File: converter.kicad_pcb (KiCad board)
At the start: 2 copper layers, 26 x 37 mm, 61 parts, among them CN1 MINI_DIN_8P_JACK, J1 USB_mini_micro_B, P1 CONN_1, P2 CONN_1, P3 CONN_1, P4 CONN_1, SW1 SW_PUSH, U1 ATMEGA32U2, X1 16MHz

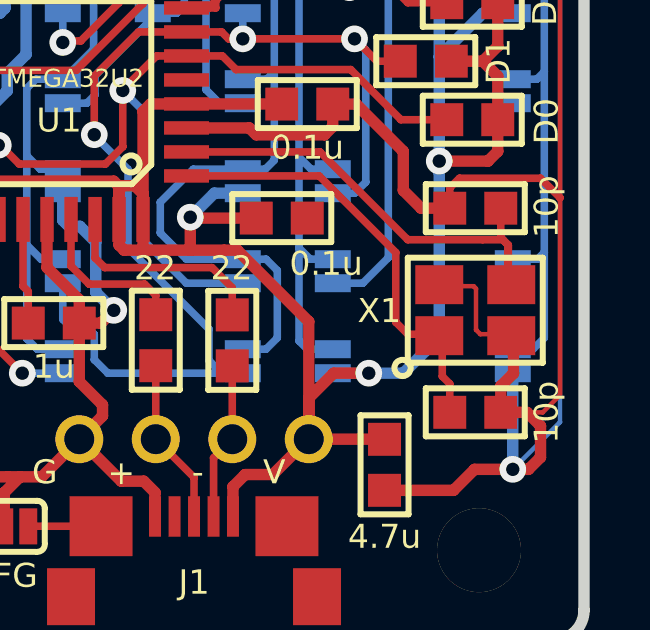
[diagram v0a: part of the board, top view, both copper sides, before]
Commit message: Change foot print of Xtal
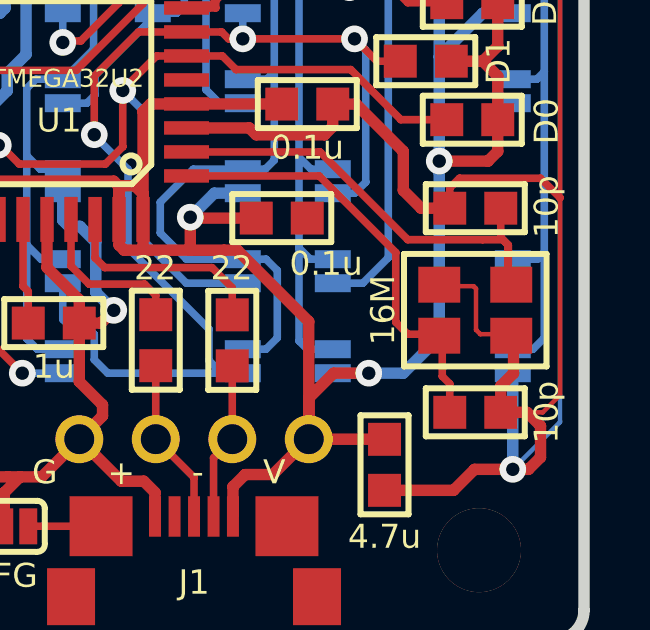
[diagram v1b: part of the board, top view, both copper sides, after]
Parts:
- X1: value 16MHz -> 16M; footprint 000NewKeyboard_parts:FA-238 -> keyboard_parts:FA-238
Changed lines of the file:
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@@
-(kicad_pcb (version 4) (host pcbnew no-vcs-found-product)
+(kicad_pcb (version 4) (host pcbnew 4.0.2+e4-6225~38~ubuntu16.04.1-stable)
   (general
     (links 112)
     (no_connects 0)
-    (area 94.297601 94.83508 130.537334 138.654001)
+    (area 94.297601 89.83508 137.637115 142.419201)
     (thickness 1.6002)
     (drawings 60)
@@
     (add_net GND)
   )
+  (module keyboard_parts:FA-238 (layer Front)
+    (at 122.375 126)
+    (fp_text reference X1 (at 0 2.55) (layer F.SilkS) hide
+      (effects (font (size 0.8 0.8) (thickness 0.15)))
+    )
+    (fp_text value 16M (at -3.075 0 90) (layer F.SilkS)
+      (effects (font (size 0.8 0.8) (thickness 0.15)))
+    )
+    (fp_line (start -2.375 1.875) (end -2.375 -1.875) (layer F.SilkS) (width 0.2))
+    (fp_line (start -2.375 -1.875) (end 2.375 -1.875) (layer F.SilkS) (width 0.2))
+    (fp_line (start 2.375 -1.875) (end 2.375 1.875) (layer F.SilkS) (width 0.2))
+    (fp_line (start 2.375 1.875) (end -2.375 1.875) (layer F.SilkS) (width 0.2))
+    (pad 3 smd rect (at -1.1 -0.8) (size 1.4 1.2) (drill (offset -0.1 -0.05)) (layers Front F.Paste F.Mask)
+      (net 31 GND) (clearance 0.2))
+    (pad 2 smd rect (at 1.1 -0.8) (size 1.4 1.2) (drill (offset 0.1 -0.05)) (layers Front F.Paste F.Mask)
+      (net 34 "Net-(C6-Pad1)") (clearance 0.2))
+    (pad 1 smd rect (at -1.1 0.8) (size 1.4 1.2) (drill (offset -0.1 0.05)) (layers Front F.Paste F.Mask)
+      (net 33 "Net-(C5-Pad1)") (clearance 0.2))
+    (pad 3 smd rect (at 1.1 0.8) (size 1.4 1.2) (drill (offset 0.1 0.05)) (layers Front F.Paste F.Mask)
+      (net 31 GND) (clearance 0.2))
+  )
   (module 000NewKeyboard_parts:QFP32 (layer Front)
     (at 108.5 118.725 180)
@@
     )
   )
-  (module 000NewKeyboard_parts:FA-238 (layer Front)
-    (at 122.375 126)
-    (fp_text reference X1 (at -3.2 0.025) (layer F.SilkS)
-      (effects (font (size 0.8 0.8) (thickness 0.15)))
-    )
-    (fp_text value 16MHz (at 0 2.775) (layer F.SilkS) hide
-      (effects (font (size 0.8 0.8) (thickness 0.15)))
-    )
-    (fp_circle (center -2.425 1.925) (end -2.65 2.075) (layer F.SilkS) (width 0.2))
-    (fp_line (start -2.25 1.725) (end -2.25 -1.75) (layer F.SilkS) (width 0.2))
-    (fp_line (start -2.25 -1.75) (end 2.25 -1.75) (layer F.SilkS) (width 0.2))
-    (fp_line (start 2.25 -1.75) (end 2.25 1.75) (layer F.SilkS) (width 0.2))
-    (fp_line (start 2.25 1.75) (end -2.25 1.75) (layer F.SilkS) (width 0.2))
-    (pad 3 smd rect (at -1.1 -0.8) (size 1.6 1.3) (drill (offset -0.1 -0.05)) (layers Front F.Paste F.Mask)
-      (net 31 GND) (clearance 0.2))
-    (pad 2 smd rect (at 1.1 -0.8) (size 1.6 1.3) (drill (offset 0.1 -0.05)) (layers Front F.Paste F.Mask)
-      (net 34 "Net-(C6-Pad1)") (clearance 0.2))
-    (pad 1 smd rect (at -1.1 0.8) (size 1.6 1.3) (drill (offset -0.1 0.05)) (layers Front F.Paste F.Mask)
-      (net 33 "Net-(C5-Pad1)") (clearance 0.2))
-    (pad 3 smd rect (at 1.1 0.8) (size 1.6 1.3) (drill (offset 0.1 0.05)) (layers Front F.Paste F.Mask)
-      (net 31 GND) (clearance 0.2))
-  )
   (module 000NewKeyboard_parts:SOLDER_JUMPER_2 (layer Front)

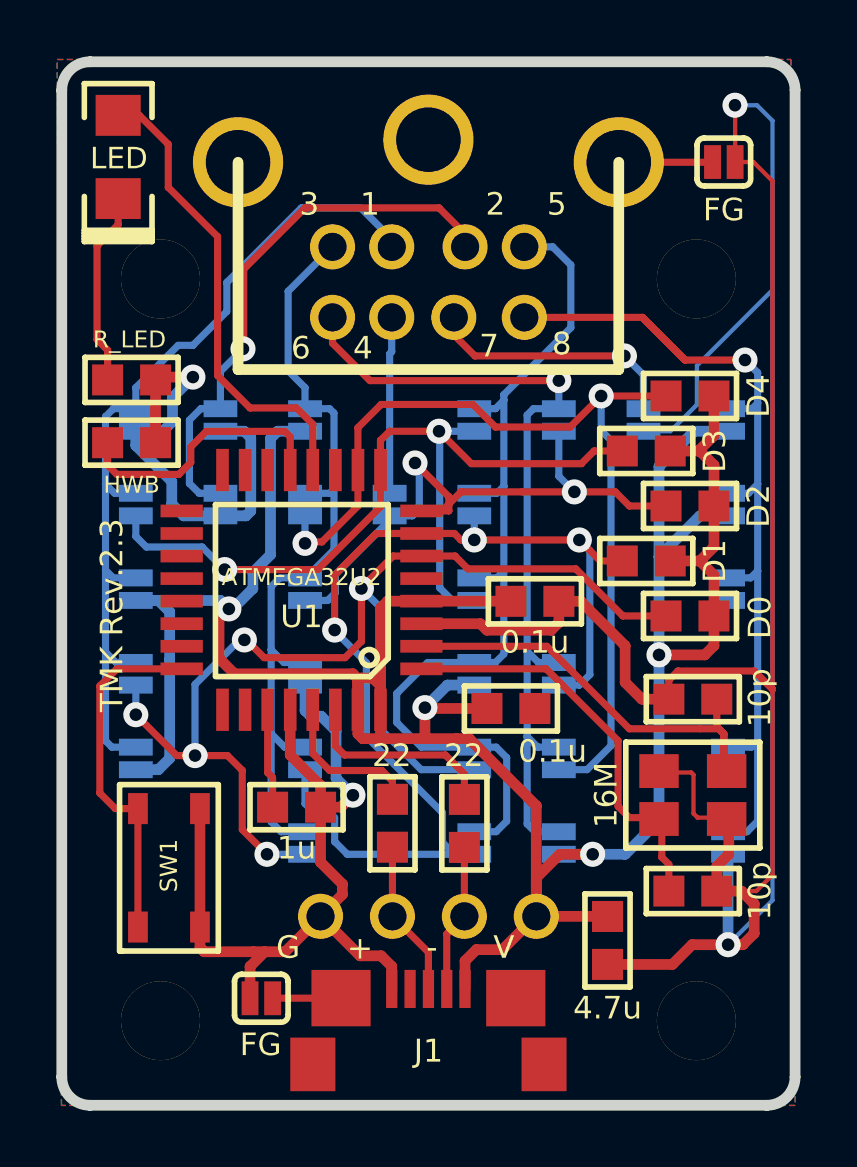
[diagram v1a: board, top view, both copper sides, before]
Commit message: Change foot print of USB_microB adding bottom pads
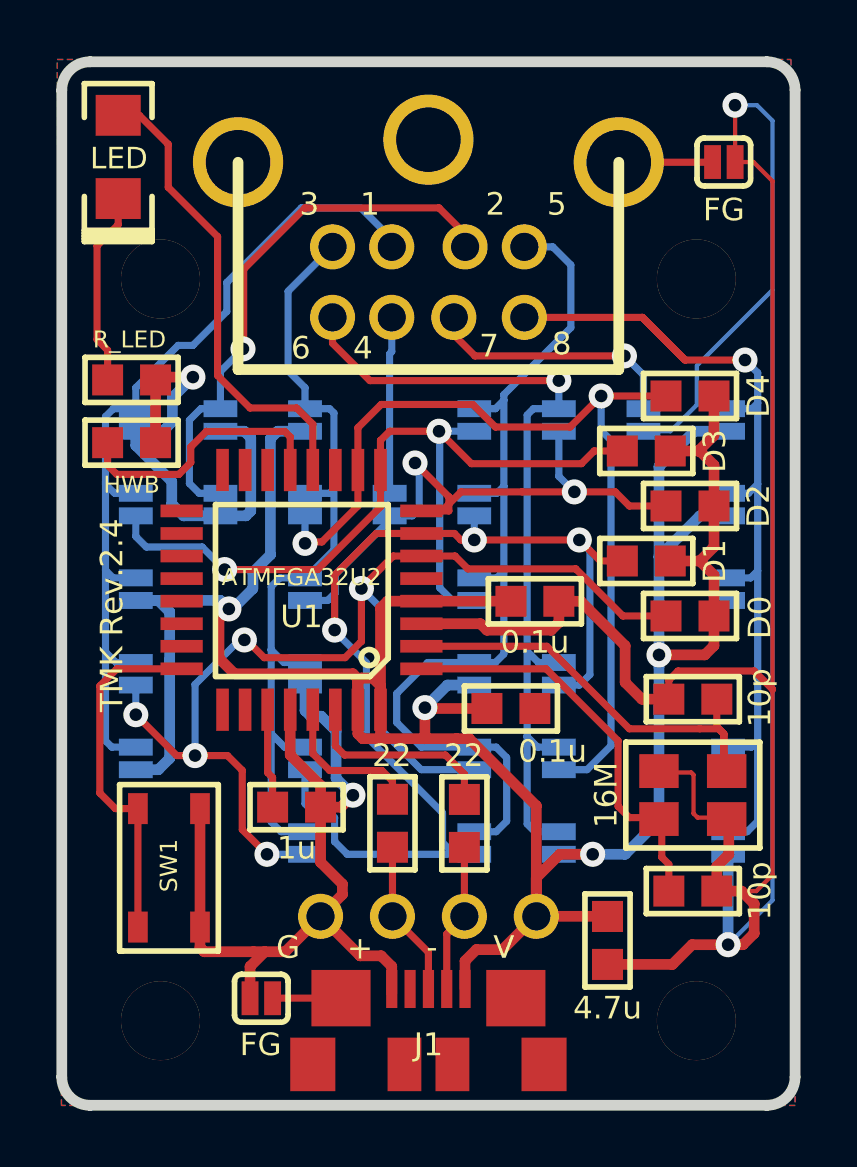
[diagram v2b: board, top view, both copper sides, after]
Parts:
- J1: footprint 000NewKeyboard_parts:USB_microB -> keyboard_parts:USB_microB
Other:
- board text added: "TMK Rev.2.4"
- board text removed: "TMK Rev.2.3"
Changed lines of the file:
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@@
   (title_block
     (title "Keyboard Protocol Converter")
-    (date 2015/12)
-    (rev 2.3)
+    (date 2016/07)
+    (rev 2.4)
     (company TMK)
   )
@@
     (mod_text_size 0.6096 0.6096)
     (mod_text_width 0.1524)
-    (pad_size 1.6 1.9)
+    (pad_size 0.6 1.2)
     (pad_drill 0)
     (pad_to_mask_clearance 0.075)
@@
     (add_net GND)
   )
+  (module keyboard_parts:USB_microB (layer Front)
+    (at 113 135.55)
+    (descr "USB microB hirose ZX62R-B-5P")
+    (tags "USB micorB hirose")
+    (fp_text reference J1 (at 0 -0.6985) (layer F.SilkS)
+      (effects (font (size 0.8128 0.8128) (thickness 0.2032)))
+    )
+    (fp_text value USB_mini_micro_B (at 0 0.22606) (layer F.SilkS) hide
+      (effects (font (size 0.6 0.6) (thickness 0.15)))
+    )
+    (fp_text user "PCB edge" (at -0.05 1.45) (layer F.SilkS) hide
+      (effects (font (size 0.5 0.5) (thickness 0.125)))
+    )
+    (fp_line (start 3.75 2.15) (end 4.25 2.75) (layer Dwgs.User) (width 0.2))
+    (fp_line (start -3.75 2.15) (end -4.25 2.675) (layer Dwgs.User) (width 0.2))
+    (fp_line (start -3 1.45) (end 3 1.45) (layer Dwgs.User) (width 0.2))
+    (fp_line (start -3.75 2.15) (end -3.75 1.35) (layer Dwgs.User) (width 0.2))
+    (fp_line (start -3.75 2.15) (end 3.75 2.15) (layer Dwgs.User) (width 0.2))
+    (fp_line (start 3.75 2.15) (end 3.75 1.35) (layer Dwgs.User) (width 0.2))
+    (pad 6 smd rect (at 0.85 0) (size 1.2 1.9) (layers Front F.Paste F.Mask))
+    (pad 1 smd rect (at 1.29794 -2.67462 180) (size 0.4 1.35) (layers Front F.Paste F.Mask)
+      (net 1 +5V) (clearance 0.1))
+    (pad 6 smd rect (at -3.0988 -2.3495) (size 2.1 2) (layers Front F.Paste F.Mask)
+      (net 43 "Net-(J1-Pad6)"))
+    (pad 6 smd rect (at 3.0988 -2.3495) (size 2.1 2) (layers Front F.Paste F.Mask))
+    (pad 6 smd rect (at -4.09956 0) (size 1.6 1.9) (layers Front F.Paste F.Mask))
+    (pad 6 smd rect (at 4.09956 0) (size 1.6 1.9) (layers Front F.Paste F.Mask))
+    (pad 2 smd rect (at 0.65024 -2.67462 180) (size 0.4 1.35) (layers Front F.Paste F.Mask)
+      (net 3 /D-) (clearance 0.1))
+    (pad 3 smd rect (at 0 -2.67462 180) (size 0.4 1.35) (layers Front F.Paste F.Mask)
+      (net 2 /D+) (clearance 0.1))
+    (pad 4 smd rect (at -0.65024 -2.67462 180) (size 0.4 1.35) (layers Front F.Paste F.Mask)
+      (net 41 "Net-(J1-Pad4)") (clearance 0.1))
+    (pad 5 smd rect (at -1.30048 -2.67462 180) (size 0.4 1.35) (layers Front F.Paste F.Mask)
+      (net 31 GND) (clearance 0.1))
+    (pad 6 smd rect (at -0.85 0) (size 1.2 1.9) (layers Front F.Paste F.Mask))
+  )
+  (module keyboard_parts:LED_3020_REFLOW (layer Front)
+    (at 102 103.375 270)
+    (descr "LED 0805 smd package")
+    (tags "LED 0805 SMD")
+    (attr smd)
+    (fp_text reference D1 (at 0 -2 270) (layer F.SilkS) hide
+      (effects (font (size 0.8 0.8) (thickness 0.15)))
+    )
+    (fp_text value LED (at 0.05 -0.025 360) (layer F.SilkS)
+      (effects (font (size 0.762 0.762) (thickness 0.127)))
+    )
+    (fp_line (start 2.9 -1.2) (end 2.9 1.2) (layer F.SilkS) (width 0.2))
+    (fp_line (start 2.8 1.2) (end 2.8 -1.2) (layer F.SilkS) (width 0.2))
+    (fp_line (start 2.7 -1.2) (end 2.7 1.2) (layer F.SilkS) (width 0.2))
+    (fp_line (start -1.4 -1.2) (end -2.6 -1.2) (layer F.SilkS) (width 0.2))
+    (fp_line (start -2.6 -1.2) (end -2.6 1.2) (layer F.SilkS) (width 0.2))
+    (fp_line (start -2.6 1.2) (end -1.4 1.2) (layer F.SilkS) (width 0.2))
+    (fp_line (start 2.6 -1.2) (end 2.6 1.2) (layer F.SilkS) (width 0.2))
+    (fp_line (start 1.4 -1.2) (end 3 -1.2) (layer F.SilkS) (width 0.2))
+    (fp_line (start 3 -1.2) (end 3 1.2) (layer F.SilkS) (width 0.2))
+    (fp_line (start 3 1.2) (end 1.4 1.2) (layer F.SilkS) (width 0.2))
+    (pad 1 smd rect (at -1.475 0 270) (size 1.45 1.6) (layers Front F.Paste F.Mask)
+      (net 28 /PD6))
+    (pad 2 smd rect (at 1.475 0 270) (size 1.45 1.6) (layers Front F.Paste F.Mask)
+      (net 35 "Net-(D1-Pad2)"))
+  )
   (module keyboard_parts:FA-238 (layer Front)
     (at 122.375 126)
@@
       (net 4 /DIN1) (clearance 0.1))
   )
-  (module 000NewKeyboard_parts:USB_microB (layer Front)
-    (at 113 135.55)
-    (descr "USB microB hirose ZX62R-B-5P")
-    (tags "USB micorB hirose")
-    (fp_text reference J1 (at 0 -0.475) (layer F.SilkS)
-      (effects (font (size 0.8128 0.8128) (thickness 0.2032)))
-    )
-    (fp_text value USB_mini_micro_B (at 0 -4.05) (layer F.SilkS) hide
-      (effects (font (size 0.6 0.6) (thickness 0.15)))
-    )
-    (fp_text user "PCB edge" (at -0.05 1.45) (layer F.SilkS) hide
-      (effects (font (size 0.5 0.5) (thickness 0.125)))
-    )
-    (fp_line (start 3.75 2.15) (end 4.25 2.75) (layer Dwgs.User) (width 0.2))
-    (fp_line (start -3.75 2.15) (end -4.25 2.675) (layer Dwgs.User) (width 0.2))
-    (fp_line (start -3 1.45) (end 3 1.45) (layer Dwgs.User) (width 0.2))
-    (fp_line (start -3.75 2.15) (end -3.75 1.35) (layer Dwgs.User) (width 0.2))
-    (fp_line (start -3.75 2.15) (end 3.75 2.15) (layer Dwgs.User) (width 0.2))
-    (fp_line (start 3.75 2.15) (end 3.75 1.35) (layer Dwgs.User) (width 0.2))
-    (pad 1 smd rect (at 1.29794 -2.67462 180) (size 0.4 1.35) (layers Front F.Paste F.Mask)
-      (net 1 +5V) (clearance 0.1))
-    (pad 6 smd rect (at -3.0988 -2.3495) (size 2.1 2) (layers Front F.Paste F.Mask)
-      (net 43 "Net-(J1-Pad6)"))
-    (pad 6 smd rect (at 3.0988 -2.3495) (size 2.1 2) (layers Front F.Paste F.Mask))
-    (pad 6 smd rect (at -4.09956 0) (size 1.6 1.9) (layers Front F.Paste F.Mask))
-    (pad 6 smd rect (at 4.09956 0) (size 1.6 1.9) (layers Front F.Paste F.Mask))
-    (pad 2 smd rect (at 0.65024 -2.67462 180) (size 0.4 1.35) (layers Front F.Paste F.Mask)
-      (net 3 /D-) (clearance 0.1))
-    (pad 3 smd rect (at 0 -2.67462 180) (size 0.4 1.35) (layers Front F.Paste F.Mask)
-      (net 2 /D+) (clearance 0.1))
-    (pad 4 smd rect (at -0.65024 -2.67462 180) (size 0.4 1.35) (layers Front F.Paste F.Mask)
-      (net 41 "Net-(J1-Pad4)") (clearance 0.1))
-    (pad 5 smd rect (at -1.30048 -2.67462 180) (size 0.4 1.35) (layers Front F.Paste F.Mask)
-      (net 31 GND) (clearance 0.1))
-  )
   (module HOLE_M2.6 (layer Front)
     (at 122.9625 133.987)
@@
     (fp_arc (start 0.7 -0.6) (end 0.7 -0.85) (angle 90) (layer F.SilkS) (width 0.2))
     (fp_arc (start 0.7 0.6) (end 0.95 0.6) (angle 90) (layer F.SilkS) (width 0.2))
-    (pad 2 smd rect (at 0.4 0) (size 0.6 1.2) (layers Front F.Paste F.Mask)
+    (pad 2 smd rect (at 0.4 0) (size 0.6 1.2) (layers Front F.Mask)
       (net 43 "Net-(J1-Pad6)") (clearance 0.1))
-    (pad 1 smd rect (at -0.4 0) (size 0.6 1.2) (layers Front F.Paste F.Mask)
+    (pad 1 smd rect (at -0.4 0) (size 0.6 1.2) (layers Front F.Mask)
       (net 31 GND) (clearance 0.1))
   )
@@
     (fp_arc (start 0.7 -0.6) (end 0.7 -0.85) (angle 90) (layer F.SilkS) (width 0.2))
     (fp_arc (start 0.7 0.6) (end 0.95 0.6) (angle 90) (layer F.SilkS) (width 0.2))
-    (pad 2 smd rect (at 0.4 0) (size 0.6 1.2) (layers Front F.Paste F.Mask)
-      (net 31 GND) (clearance 0.1))
-    (pad 1 smd rect (at -0.4 0) (size 0.6 1.2) (layers Front F.Paste F.Mask)
+    (pad 2 smd rect (at 0.4 0) (size 0.6 1.2) (layers Front F.Mask)
+      (net 31 GND) (clearance 0.1))
+    (pad 1 smd rect (at -0.4 0) (size 0.6 1.2) (layers Front F.Mask)
       (net 42 "Net-(CN1-Pad9)") (clearance 0.1))
   )
@@
       (net 10 /DIN7))
   )
-  (module keyboard_parts:LED_3020_REFLOW (layer Front)
-    (at 102 103.375 270)
-    (descr "LED 0805 smd package")
-    (tags "LED 0805 SMD")
-    (attr smd)
-    (fp_text reference D1 (at 0 -2 270) (layer F.SilkS) hide
-      (effects (font (size 0.8 0.8) (thickness 0.15)))
-    )
-    (fp_text value LED (at 0.05 -0.025 360) (layer F.SilkS)
-      (effects (font (size 0.762 0.762) (thickness 0.127)))
-    )
-    (fp_line (start 2.9 -1.2) (end 2.9 1.2) (layer F.SilkS) (width 0.2))
-    (fp_line (start 2.8 1.2) (end 2.8 -1.2) (layer F.SilkS) (width 0.2))
-    (fp_line (start 2.7 -1.2) (end 2.7 1.2) (layer F.SilkS) (width 0.2))
-    (fp_line (start -1.4 -1.2) (end -2.6 -1.2) (layer F.SilkS) (width 0.2))
-    (fp_line (start -2.6 -1.2) (end -2.6 1.2) (layer F.SilkS) (width 0.2))
-    (fp_line (start -2.6 1.2) (end -1.4 1.2) (layer F.SilkS) (width 0.2))
-    (fp_line (start 2.6 -1.2) (end 2.6 1.2) (layer F.SilkS) (width 0.2))
-    (fp_line (start 1.4 -1.2) (end 3 -1.2) (layer F.SilkS) (width 0.2))
-    (fp_line (start 3 -1.2) (end 3 1.2) (layer F.SilkS) (width 0.2))
-    (fp_line (start 3 1.2) (end 1.4 1.2) (layer F.SilkS) (width 0.2))
-    (pad 1 smd rect (at -1.475 0 270) (size 1.45 1.6) (layers Front F.Paste F.Mask)
-      (net 28 /PD6))
-    (pad 2 smd rect (at 1.475 0 270) (size 1.45 1.6) (layers Front F.Paste F.Mask)
-      (net 35 "Net-(D1-Pad2)"))
-  )
   (dimension 7.7 (width 0.1524) (layer Dwgs.User)
     (gr_text "7.700 mm" (at 135.2096 103.85 90) (layer Dwgs.User)
@@
     (arrow2b (pts (xy 122.5 91.1) (xy 121.373496 91.686421)))
   )
-  (gr_text "TMK Rev.2.3" (at 101.775 119.625 90) (layer F.SilkS)
+  (gr_text "TMK Rev.2.4" (at 101.775 119.625 90) (layer F.SilkS)
     (effects (font (size 0.8 0.8) (thickness 0.15)))
   )
